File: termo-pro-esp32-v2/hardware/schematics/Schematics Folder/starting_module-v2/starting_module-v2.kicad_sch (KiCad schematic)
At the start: 17 parts, among them J1 Screw_Terminal_01x02, J2 Screw_Terminal_01x02, J3 Conn_01x08_Pin, K1 SANYOU_SRD_Form_C, Q1 PN2222A, SW1 SW_Push_LED, U2 ESP32-C3_SUPERMINI_TH

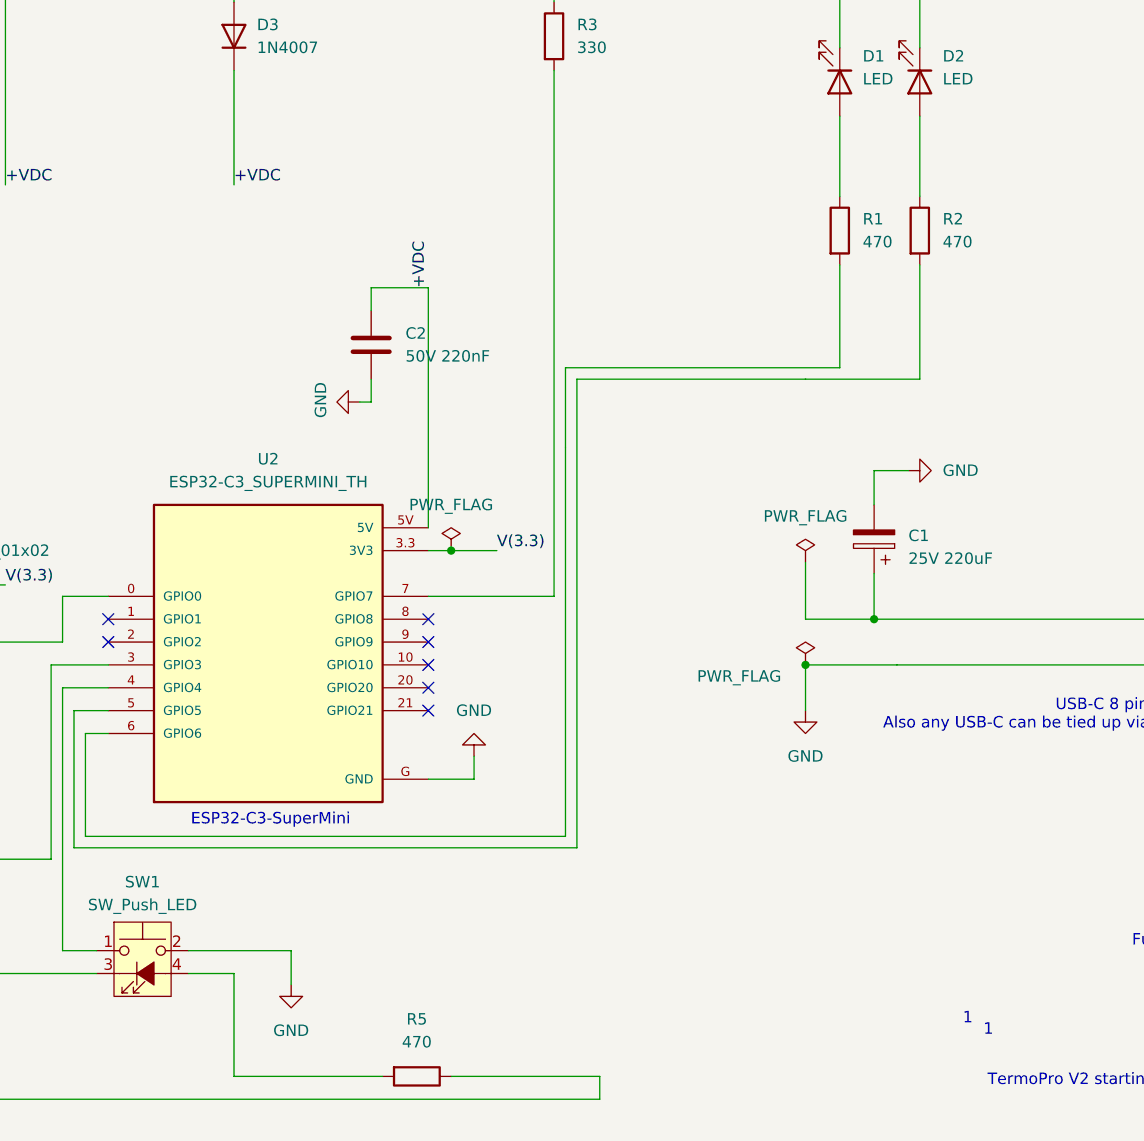
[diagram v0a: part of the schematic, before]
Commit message: Hardware part of the project is finished.
-DHT11 placement on thermostat unit fixed, pins trace redone.
-USB-C port on thermostat unit placed closer to edge by 4mm.
-Capacitors values recalculated and updated to closest common values, resistors values too.
-Starting unit pcb redone traces as relay and caps have been moved to the back plate.

-Starting & thermostat units PCB are done, inspected.
-Ready for fabrication.
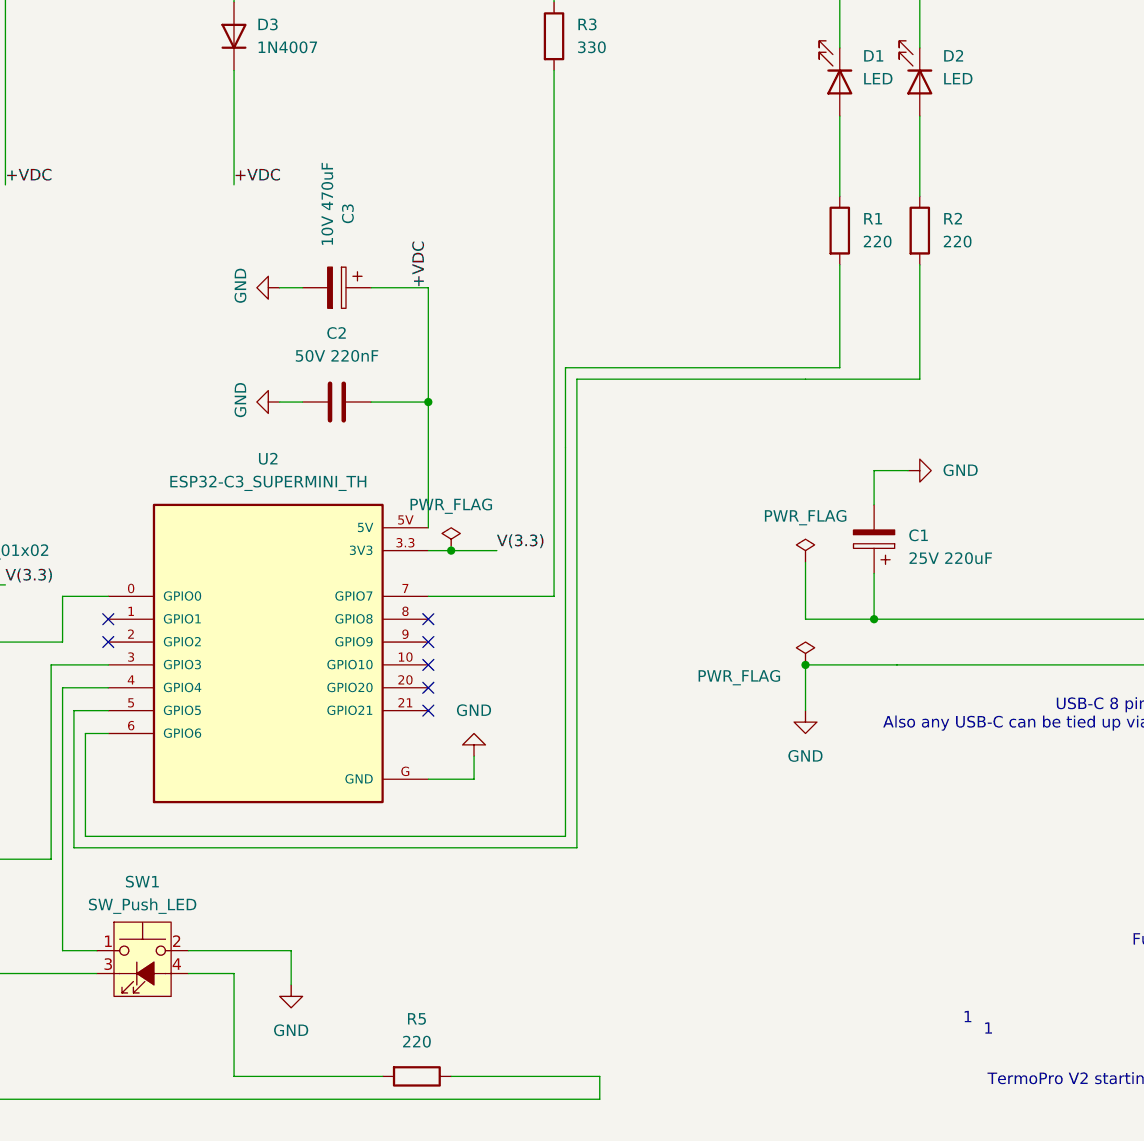
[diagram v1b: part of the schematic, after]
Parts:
- added C3: 10V 470uF, Capacitor_THT:CP_Radial_D8.0mm_P5.00mm, symbol Device:C_Polarized
- R1, R2, R5: value 470 -> 220
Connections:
- net +VDC: now also C2.1, C3.1; no longer C2.2
- net GND: now also C2.2, C3.2; no longer C2.1
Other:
- note removed: "ESP32-C3-SuperMini"
- moved on the sheet: C2
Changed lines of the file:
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@@
 	(generator_version "10.0")
 	(paper "A4")
-	(text "ESP32-C3-SuperMini"
-		(exclude_from_sim no)
-		(at 108.204 160.782 0)
-		(effects
-			(font
-				(size 1.27 1.27)
-			)
-		)
-	)
 	(text "1\n"
 		(exclude_from_sim no)
@@
 	)
 	(junction
+		(at 125.73 114.3)
+		(diameter 0)
+		(color 0 0 0 0)
+	)
+	(junction
 		(at 180.34 60.96)
 		(diameter 0)
@@
 	(wire
 		(pts
+			(xy 111.76 101.6) (xy 109.22 101.6)
+		)
+		(stroke
+			(width 0)
+			(type default)
+			(color 0 0 255 1)
+		)
+	)
+	(wire
+		(pts
 			(xy 119.38 101.6) (xy 125.73 101.6)
 		)
@@
 	(wire
 		(pts
-			(xy 125.73 101.6) (xy 125.73 128.27)
+			(xy 125.73 101.6) (xy 125.73 114.3)
 		)
 		(stroke
@@
 	(wire
 		(pts
-			(xy 119.38 114.3) (xy 119.38 111.76)
-		)
-		(stroke
-			(width 0)
-			(type default)
-			(color 0 0 255 1)
-		)
-	)
-	(wire
-		(pts
 			(xy 85.09 175.26) (xy 88.9 175.26)
 		)
@@
 	(wire
 		(pts
+			(xy 125.73 114.3) (xy 125.73 128.27)
+		)
+		(stroke
+			(width 0)
+			(type default)
+			(color 255 0 0 1)
+		)
+	)
+	(wire
+		(pts
 			(xy 83.82 165.1) (xy 83.82 143.51)
 		)
@@
 	(wire
 		(pts
-			(xy 119.38 101.6) (xy 119.38 104.14)
-		)
-		(stroke
-			(width 0)
-			(type default)
-			(color 255 0 0 1)
-		)
-	)
-	(wire
-		(pts
 			(xy 63.5 165.1) (xy 83.82 165.1)
 		)
@@
 	(wire
 		(pts
+			(xy 119.38 114.3) (xy 125.73 114.3)
+		)
+		(stroke
+			(width 0)
+			(type default)
+			(color 255 0 0 1)
+		)
+	)
+	(wire
+		(pts
 			(xy 175.26 125.73) (xy 175.26 121.92)
 		)
@@
 	(wire
 		(pts
-			(xy 119.38 114.3) (xy 118.11 114.3)
+			(xy 111.76 114.3) (xy 109.22 114.3)
 		)
 		(stroke
@@
 			)
 		)
-		(property "Value" "470"
+		(property "Value" "220"
 			(at 182.88 96.5199 0)
 			(show_name no)
@@
 	(symbol
 		(lib_id "power:GND")
-		(at 118.11 114.3 270)
+		(at 109.22 114.3 270)
 		(unit 1)
 		(body_style 1)
@@
 		(dnp no)
 		(property "Reference" "#PWR014"
-			(at 111.76 114.3 0)
+			(at 102.87 114.3 0)
 			(hide yes)
 			(show_name no)
@@
 		)
 		(property "Value" "GND"
-			(at 113.792 116.078 0)
+			(at 104.902 116.078 0)
 			(show_name no)
 			(do_not_autoplace no)
@@
 		)
 		(property "Footprint" ""
-			(at 118.11 114.3 0)
+			(at 109.22 114.3 0)
 			(hide yes)
 			(show_name no)
@@
 		)
 		(property "Datasheet" ""
-			(at 118.11 114.3 0)
+			(at 109.22 114.3 0)
 			(hide yes)
 			(show_name no)
@@
 		)
 		(property "Description" "Power symbol creates a global label with name \"GND\" , ground"
-			(at 118.11 114.3 0)
+			(at 109.22 114.3 0)
 			(hide yes)
 			(show_name no)
@@
 			)
 		)
-		(property "Value" "470"
+		(property "Value" "220"
 			(at 124.46 185.42 90)
 			(show_name no)
@@
 	(symbol
 		(lib_id "power:GND")
+		(at 109.22 101.6 270)
+		(unit 1)
+		(body_style 1)
+		(exclude_from_sim no)
+		(in_bom yes)
+		(on_board yes)
+		(in_pos_files yes)
+		(dnp no)
+		(property "Reference" "#PWR015"
+			(at 102.87 101.6 0)
+			(hide yes)
+			(show_name no)
+			(do_not_autoplace no)
+			(effects
+				(font
+					(size 1.27 1.27)
+				)
+			)
+		)
+		(property "Value" "GND"
+			(at 104.902 103.378 0)
+			(show_name no)
+			(do_not_autoplace no)
+			(effects
+				(font
+					(size 1.27 1.27)
+				)
+				(justify right)
+			)
+		)
+		(property "Footprint" ""
+			(at 109.22 101.6 0)
+			(hide yes)
+			(show_name no)
+			(do_not_autoplace no)
+			(effects
+				(font
+					(size 1.27 1.27)
+				)
+			)
+		)
+		(property "Datasheet" ""
+			(at 109.22 101.6 0)
+			(hide yes)
+			(show_name no)
+			(do_not_autoplace no)
+			(effects
+				(font
+					(size 1.27 1.27)
+				)
+			)
+		)
+		(property "Description" "Power symbol creates a global label with name \"GND\" , ground"
+			(at 109.22 101.6 0)
+			(hide yes)
+			(show_name no)
+			(do_not_autoplace no)
+			(effects
+				(font
+					(size 1.27 1.27)
+				)
+			)
+		)
+		(pin "1"
+		)
+		(instances
+			(project "starting_module-v2"
+				(path "/afbf1656-3cc8-4ba3-a780-b64b3df023f3"
+					(reference "#PWR015")
+					(unit 1)
+				)
+			)
+		)
+	)
+	(symbol
+		(lib_id "power:GND")
 		(at 167.64 148.59 0)
 		(unit 1)
@@
 	(symbol
 		(lib_id "Device:C")
-		(at 119.38 107.95 180)
+		(at 115.57 114.3 270)
 		(unit 1)
 		(body_style 1)
@@
 		(fields_autoplaced yes)
 		(property "Reference" "C2"
-			(at 123.19 106.6799 0)
+			(at 115.57 106.68 90)
 			(show_name no)
 			(do_not_autoplace no)
@@
 					(size 1.27 1.27)
 				)
-				(justify right)
 			)
 		)
 		(property "Value" "50V 220nF"
-			(at 123.19 109.2199 0)
+			(at 115.57 109.22 90)
 			(show_name no)
 			(do_not_autoplace no)
@@
 					(size 1.27 1.27)
 				)
-				(justify right)
 			)
 		)
 		(property "Footprint" "Capacitor_THT:C_Disc_D11.0mm_W5.0mm_P5.00mm"
-			(at 118.4148 104.14 0)
+			(at 111.76 115.2652 0)
 			(hide yes)
 			(show_name no)
@@
 		)
 		(property "Datasheet" ""
-			(at 119.38 107.95 0)
+			(at 115.57 114.3 0)
 			(hide yes)
 			(show_name no)
@@
 		)
 		(property "Description" "Unpolarized capacitor"
-			(at 119.38 107.95 0)
+			(at 115.57 114.3 0)
 			(hide yes)
 			(show_name no)
@@
 			)
 		)
-		(property "Value" "470"
+		(property "Value" "220"
 			(at 173.99 96.5199 0)
 			(show_name no)
@@
 					(unit 1)
 				)
+			)
+		)
+	)
+	(symbol
+		(lib_id "Device:C_Polarized")
+		(at 115.57 101.6 270)
+		(unit 1)
+		(body_style 1)
+		(exclude_from_sim no)
+		(in_bom yes)
+		(on_board yes)
+		(in_pos_files yes)
+		(dnp no)
+		(property "Reference" "C3"
+			(at 116.84 92.202 0)
+			(show_name no)
+			(do_not_autoplace no)
+			(effects
+				(font
+					(size 1.27 1.27)
+				)
+				(justify left)
+			)
+		)
+		(property "Value" "10V 470uF"
+			(at 114.554 87.63 0)
+			(show_name no)
+			(do_not_autoplace no)
+			(effects
+				(font
+					(size 1.27 1.27)
+				)
+				(justify left)
+			)
+		)
+		(property "Footprint" "Capacitor_THT:CP_Radial_D8.0mm_P5.00mm"
+			(at 111.76 102.5652 0)
+			(hide yes)
+			(show_name no)
+			(do_not_autoplace no)
+			(effects
+				(font
+					(size 1.27 1.27)
+				)
+			)
+		)
+		(property "Datasheet" ""
+			(at 115.57 101.6 0)
+			(hide yes)
+			(show_name no)
+			(do_not_autoplace no)
+			(effects
+				(font
+					(size 1.27 1.27)
+				)
+			)
+		)
+		(property "Description" "Polarized capacitor"
+			(at 115.57 101.6 0)
+			(hide yes)
+			(show_name no)
+			(do_not_autoplace no)
+			(effects
+				(font
+					(size 1.27 1.27)
+				)
+			)
+		)
+		(pin "1"
+		)
+		(pin "2"
+		)
+		(instances
+			(project "starting_module-v2"
+				(path "/afbf1656-3cc8-4ba3-a780-b64b3df023f3"
+					(reference "C3")
+					(unit 1)
+				)
